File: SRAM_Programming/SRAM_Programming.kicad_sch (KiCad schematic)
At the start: 3 parts, among them SW1 SW_DIP_x08, U1 IS62C256AL

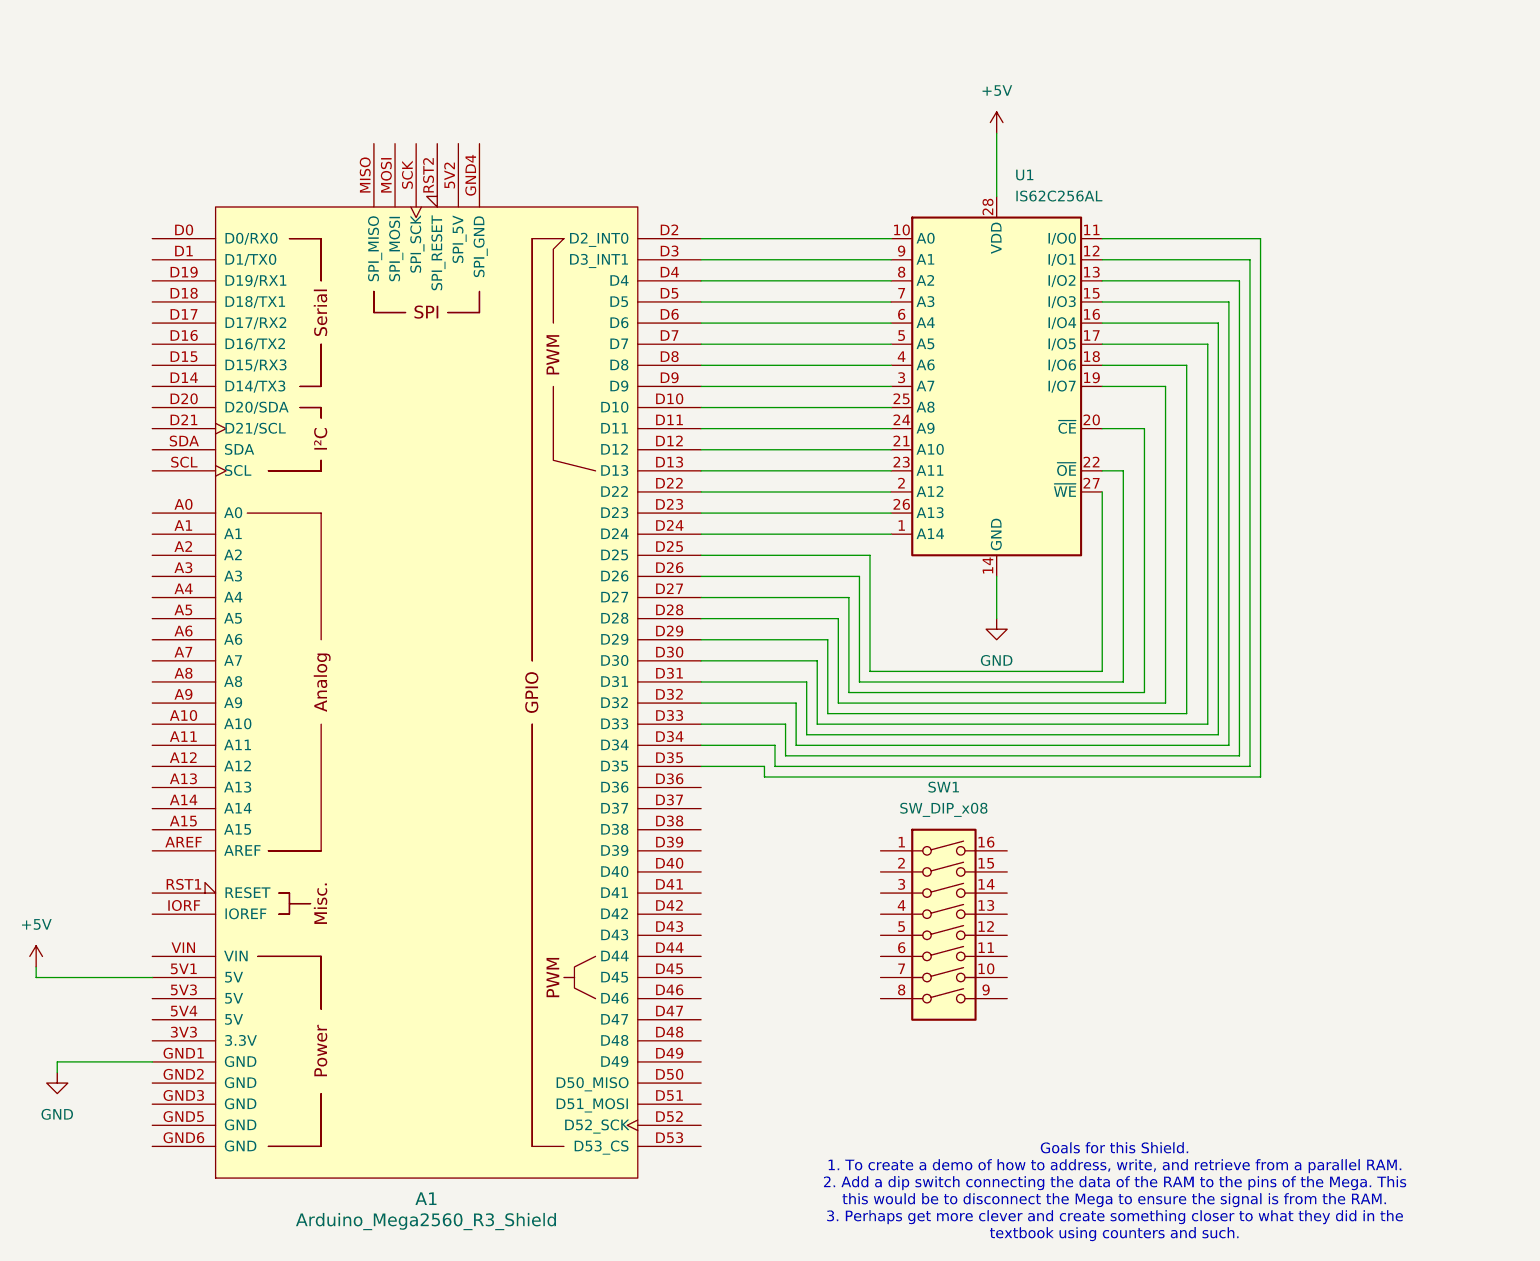
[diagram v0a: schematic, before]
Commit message: started pcb layout
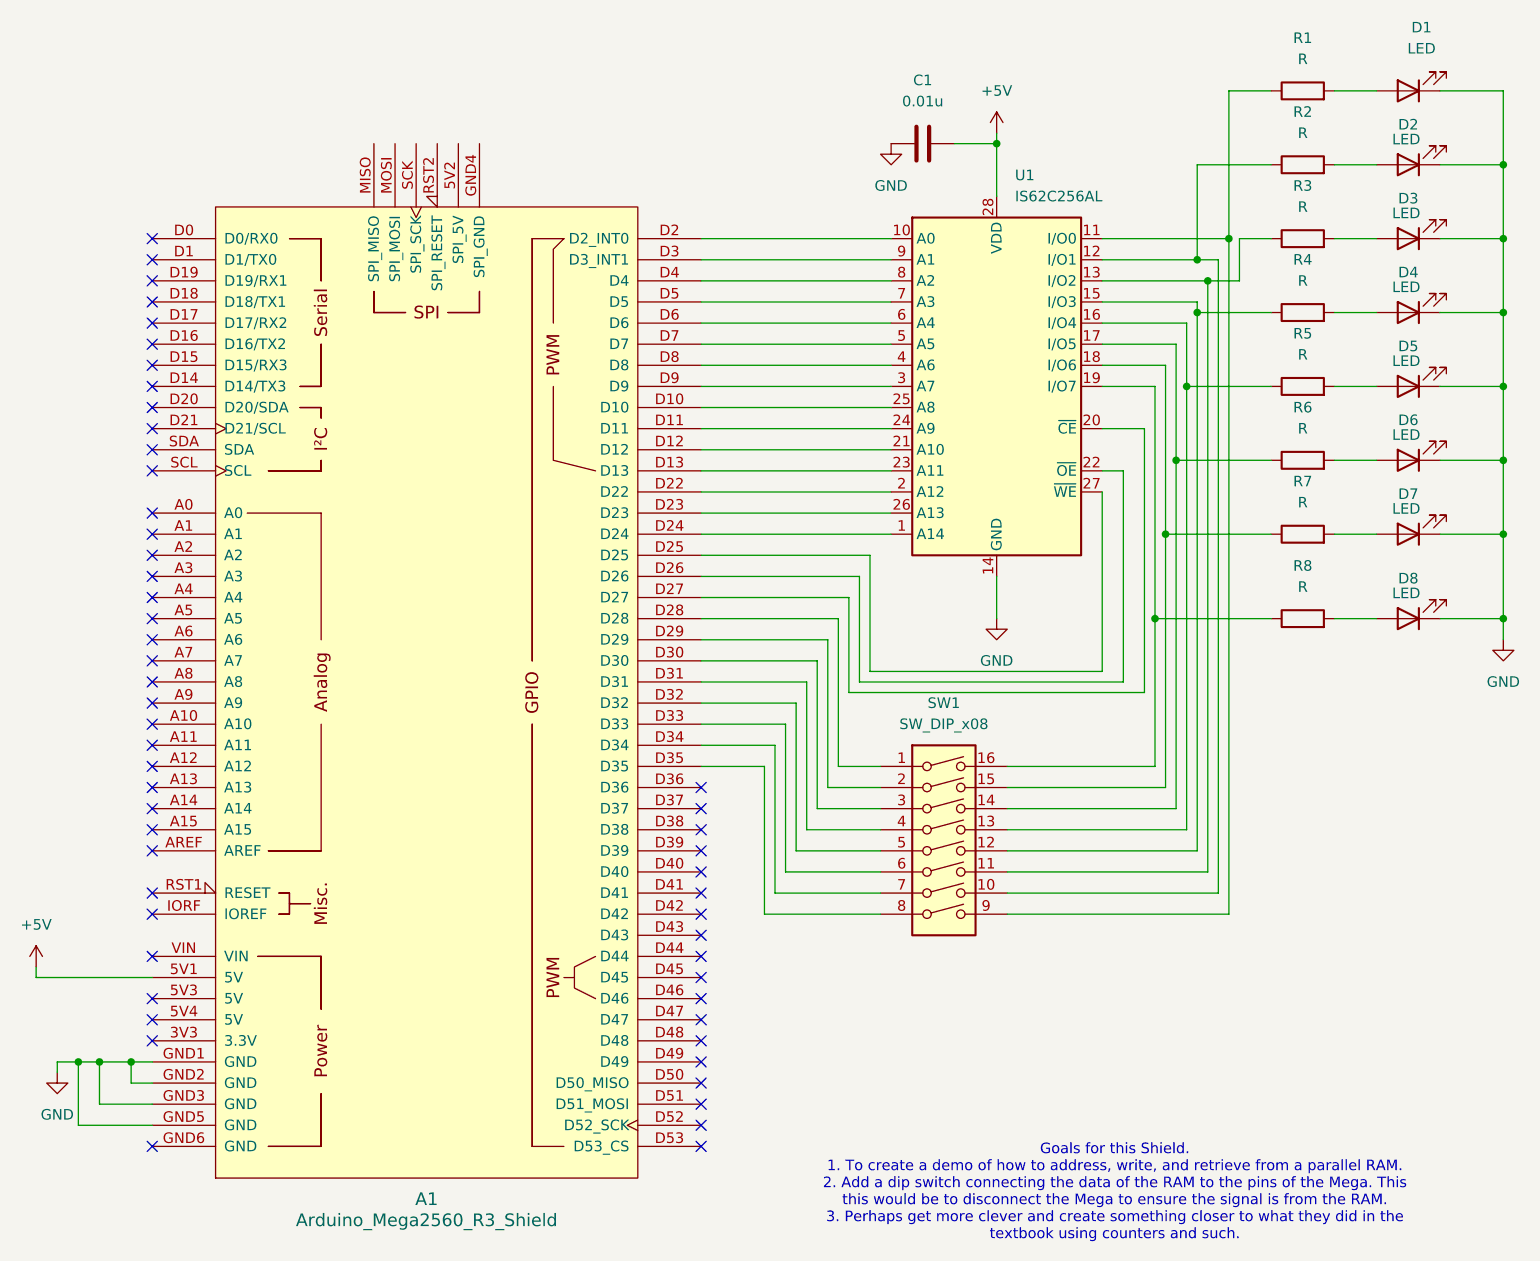
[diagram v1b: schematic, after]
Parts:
- added C1: 0.01u, Capacitor_SMD:C_0805_2012Metric_Pad1.18x1.45mm_HandSolder, symbol Device:C
- added D1, D2, D3, D4, D5, D6, D7, D8: LED, LED_THT:LED_D5.0mm, symbol Device:LED
- added R1, R2, R3, R4, R5, R6, R7, R8: R, Resistor_THT:R_Axial_DIN0309_L9.0mm_D3.2mm_P12.70mm_Horizontal, symbol Device:R
- SW1: footprint (none) -> Button_Switch_THT:SW_DIP_SPSTx08_Slide_6.7x21.88mm_W7.62mm_P2.54mm_LowProfile; MfG # (none) -> 208-8
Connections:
- net +5V: now also C1.1
- net GND: now also A1.GND2 (GND), A1.GND3 (GND), A1.GND5 (GND), C1.2, D1.1 (K), D2.1 (K), D3.1 (K), D4.1 (K), D5.1 (K), D6.1 (K), D7.1 (K), D8.1 (K)
- net at U1.19 (I/O7): now also SW1.16, R8.1; no longer A1.D28
- net at U1.18 (I/O6): now also SW1.15, R7.1; no longer A1.D29
- net at A1.D30: now also SW1.3; no longer U1.17 (I/O5)
- net at A1.D31: now also SW1.4; no longer U1.16 (I/O4)
- net at U1.15 (I/O3): now also SW1.12, R4.1; no longer A1.D32
- net at A1.D33: now also SW1.6; no longer U1.13 (I/O2)
- net at A1.D34: now also SW1.7; no longer U1.12 (I/O1)
- net at U1.11 (I/O0): now also SW1.9, R1.1; no longer A1.D35
- net at SW1.1: now also A1.D28
- net at SW1.10: now also U1.12 (I/O1), R2.1
- net at SW1.11: now also U1.13 (I/O2), R3.1
- net at SW1.13: now also U1.16 (I/O4), R5.1
- net at SW1.14: now also U1.17 (I/O5), R6.1
- net at SW1.2: now also A1.D29
- net at SW1.5: now also A1.D32
- net at SW1.8: now also A1.D35
- new net: D7.2 (A), R7.2
- new net: D4.2 (A), R4.2
- new net: D8.2 (A), R8.2
- new net: D1.2 (A), R1.2
- new net: D5.2 (A), R5.2
- new net: D3.2 (A), R3.2
- new net: D6.2 (A), R6.2
- new net: D2.2 (A), R2.2
- no-connect marks 0 -> 54
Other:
- moved on the sheet: SW1
